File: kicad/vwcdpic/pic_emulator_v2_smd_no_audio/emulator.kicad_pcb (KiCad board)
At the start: 2 copper layers, 24.1 x 18.4 mm, 12 parts, among them P1 CONN_01X05, P2 CONN_01X02, U1 PIC12F629, U2 78L05

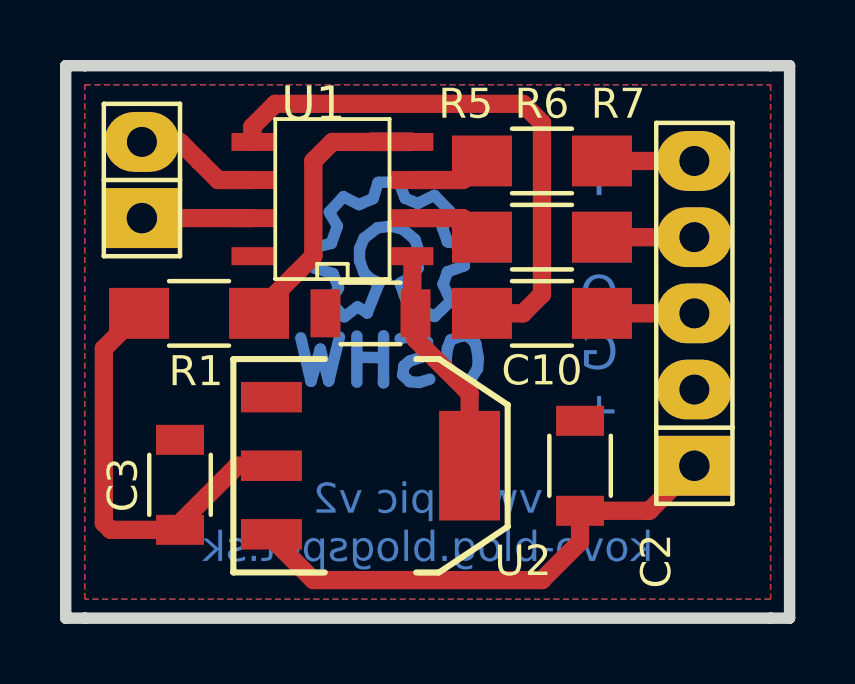
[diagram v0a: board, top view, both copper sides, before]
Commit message: update pcb with soic8 handsoldering module
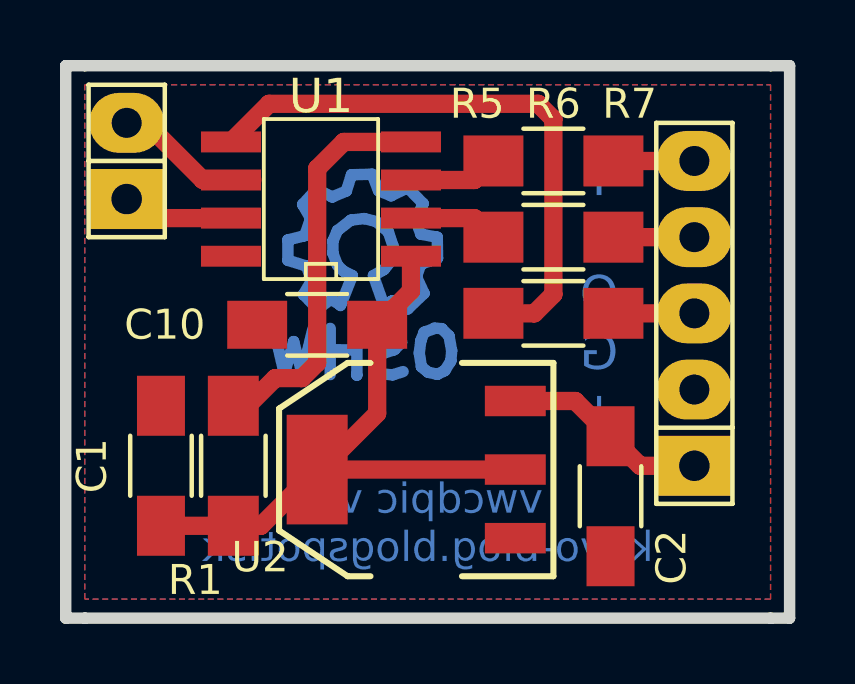
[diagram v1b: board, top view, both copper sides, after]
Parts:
- removed C3: 100n, Capacitors_SMD:C_1206
- added C1: 100n, Capacitors_SMD:C_1206_HandSoldering, F.Cu at (94.0, 57.8)
- C10, C2: footprint Capacitors_SMD:C_1206 -> Capacitors_SMD:C_1206_HandSoldering
- U1: footprint SMD_Packages:SOIC-8-W -> my_modules:SOIC-8-W_long_pads
- moved R1 5.21 mm to (96.4, 57.8), turned to 270 degrees
- moved C10 1.82 mm to (99.2, 53.1)
- moved U2 1.53 mm to (102.5, 57.9), turned to 90 degrees
- moved C2 1.44 mm to (109.0, 58.8), turned to 270 degrees
- moved SYM 0.92 mm to (100.7, 50.5)
- moved P2 0.81 mm to (92.8, 47.6)
- moved R5 0.38 mm to (107.1, 50.2)
- moved R6 0.38 mm to (107.1, 47.6)
- moved R7 0.38 mm to (107.1, 52.7)
- moved U1 0.38 mm to (99.3, 48.9)
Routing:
- net POWER_CTL: track 17.3 -> 7.75 mm
- net Net-(R1-Pad1): track 12.3 -> 14.1 mm
- net Net-(P2-Pad2): track 4.21 -> 5.41 mm
- net +5V: track 22.5 -> 21.3 mm
- net Net-(R7-Pad1): track 18.7 -> 19.6 mm

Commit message: smd boards update: singleside smd, doubleside smd, minimized
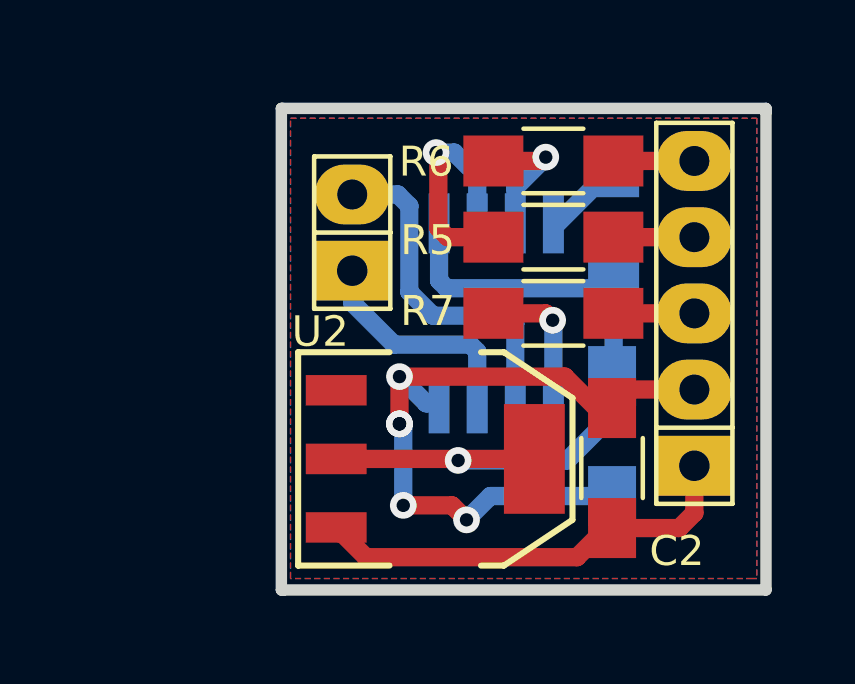
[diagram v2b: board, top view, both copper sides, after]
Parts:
- removed C10: 100n, Capacitors_SMD:C_1206_HandSoldering
- removed SYM: Symbol_OSHW-Logo_CopperTop_07Jul2012, Symbols:Symbol_OSHW-Logo_CopperTop
- C1, R1, U1: moved to B.Cu
- moved C1 15.1 mm to (109.0, 56.8), turned to 270 degrees
- moved R1 15.0 mm to (109.1, 49.8)
- moved P2 7.89 mm to (100.4, 50.0)
- moved U1 6.97 mm to (105.2, 52.7), turned to 0 degrees
- moved C2 0.94 mm to (109.0, 57.9), turned to 90 degrees
- moved U2 0.73 mm to (103.1, 57.6), turned to 270 degrees
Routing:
- net GND: track 0.22 -> 24.0 mm, vias 0 -> 5
- net Net-(R7-Pad1): track 19.6 -> 4.85 mm, vias 0 -> 1
- net Net-(R1-Pad1): track 14.1 -> 2.78 mm
- net POWER_CTL: track 7.75 -> 14.5 mm
- net Net-(P2-Pad2): track 5.41 -> 11.6 mm
- net Net-(R5-Pad1): track 3.01 -> 7.79 mm, vias 0 -> 1
- net Net-(P2-Pad1): track 3.74 -> 7.64 mm
- net +5V: track 21.3 -> 24.6 mm, vias 0 -> 1
- net Net-(R6-Pad1): track 3.01 -> 4.43 mm, vias 0 -> 1
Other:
- board size 24.1 x 18.4 mm -> 16.2 x 16.1 mm

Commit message: ICSP header added, serial header deleted, serial pins are on ICSP header
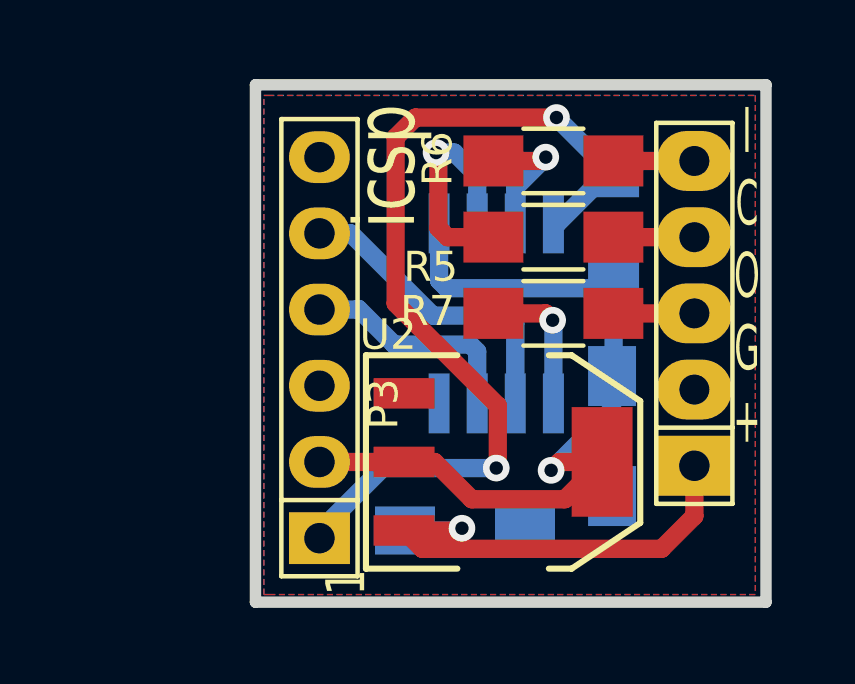
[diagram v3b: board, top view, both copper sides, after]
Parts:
- removed P2: CONN_01X02, Pin_Headers:Pin_Header_Straight_1x02
- added P3: CONN_01X06, Pin_Headers:Pin_Header_Straight_1x06, F.Cu at (99.3, 53.8)
- C2: moved to B.Cu
- moved C2 5.33 mm to (104.1, 59.9), turned to 0 degrees
- moved U2 2.26 mm to (105.4, 57.7)
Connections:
- net Net-(R1-Pad1) renamed /ICSP_VPP
- U1 pad 6: Net-(P2-Pad2) -> /ICSP_CLK
- U1 pad 7: Net-(P2-Pad1) -> /ICSP_DATA
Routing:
- net /ICSP_VPP: track 2.78 -> 30.5 mm, vias 0 -> 2
- net GND: track 24.0 -> 0.00 mm, vias 5 -> 0
- net Net-(P2-Pad2): track 11.6 -> 0.00 mm
- net /ICSP_CLK: track 0.00 -> 10.4 mm
- net Net-(P2-Pad1): track 7.64 -> 0.00 mm
- net /ICSP_DATA: track 0.00 -> 7.59 mm
- net +5V: track 24.6 -> 27.0 mm
- net POWER_CTL: track 14.5 -> 16.0 mm, vias 0 -> 1
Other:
- board size 16.2 x 16.1 mm -> 17 x 17.2 mm
- board text added: "1"
- board text added: "icsp"
- board text added: "kovo-blog.blogspot.sk vwcdpic v2"
- board text removed: "vwcdpic v2 kovo-blog.blogspot.sk"
